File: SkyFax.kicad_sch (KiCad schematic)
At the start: 8 parts, among them J1 RJ11/12, J4 Conn_02x08_Odd_Even, J5 Conn_01x02, J6 Conn_01x02

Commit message: Sent to fab v3.0
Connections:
- net GND: now also J4.16 (Pin_16); no longer J4.15 (Pin_15)
- net SI2494/3V3: now also J4.2 (Pin_2); no longer J4.1 (Pin_1)
- net SI2494/CTS: now also J4.10 (Pin_10); no longer J4.9 (Pin_9)
- net SI2494/DCD: now also J4.14 (Pin_14); no longer J4.13 (Pin_13)
- net SI2494/RI: now also J4.12 (Pin_12); no longer J4.11 (Pin_11)
- net SI2494/RTS: now also J4.8 (Pin_8); no longer J4.7 (Pin_7)
- net SI2494/RXD: now also J4.6 (Pin_6); no longer J4.5 (Pin_5)
- net SI2494/TXD: now also J4.4 (Pin_4); no longer J4.3 (Pin_3)
- net SI3018/RING: now also J1.4, J6.1 (Pin_1); no longer J1.3, J6.2 (Pin_2)
- net SI3018/TIP: now also J1.3, J6.2 (Pin_2); no longer J1.4, J6.1 (Pin_1)
- net USB_Serial/3V3: now also J4.1 (Pin_1); no longer J4.2 (Pin_2)
- net USB_Serial/CTS: now also J4.9 (Pin_9); no longer J4.10 (Pin_10)
- net USB_Serial/DCD: now also J4.13 (Pin_13); no longer J4.14 (Pin_14)
- net USB_Serial/GND: now also J4.15 (Pin_15); no longer J4.16 (Pin_16)
- net USB_Serial/RI: now also J4.11 (Pin_11); no longer J4.12 (Pin_12)
- net USB_Serial/RTS: now also J4.7 (Pin_7); no longer J4.8 (Pin_8)
- net USB_Serial/RXD: now also J4.5 (Pin_5); no longer J4.6 (Pin_6)
- net USB_Serial/TXD: now also J4.3 (Pin_3); no longer J4.4 (Pin_4)
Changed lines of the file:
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@@
+    (stroke (width 0) (type default))
+  )
+  (wire (pts (xy 50.8 47.625) (xy 52.07 47.625))
+    (stroke (width 0) (type default))
+  )
+  (wire (pts (xy 84.455 41.91) (xy 85.09 41.91))
+    (stroke (width 0) (type default))
+  )
+  (wire (pts (xy 48.895 41.91) (xy 52.07 41.91))
+    (stroke (width 0) (type default))
+  )
+  (wire (pts (xy 84.455 30.48) (xy 84.455 41.91))
+    (stroke (width 0) (type default))
+  )
+  (wire (pts (xy 65.405 38.735) (xy 66.04 38.735))
+    (stroke (width 0) (type default))
+  )
+  (wire (pts (xy 33.655 47.625) (xy 35.56 47.625))
+    (stroke (width 0) (type default))
+  )
+  (wire (pts (xy 50.165 32.385) (xy 50.165 34.29))
+    (stroke (width 0) (type default))
+  )
+  (wire (pts (xy 48.26 32.385) (xy 50.165 32.385))
+    (stroke (width 0) (type default))
+  )
+  (wire (pts (xy 34.925 37.465) (xy 35.56 37.465))
+    (stroke (width 0) (type default))
+  )
+  (wire (pts (xy 31.75 36.195) (xy 34.29 36.195))
+    (stroke (width 0) (type default))
+  )
+  (wire (pts (xy 48.26 34.925) (xy 49.53 34.925))
+    (stroke (width 0) (type default))
+  )
+  (wire (pts (xy 48.895 37.465) (xy 48.895 38.1))
+    (stroke (width 0) (type default))
+  )
+  (wire (pts (xy 49.53 45.085) (xy 49.53 43.815))
+    (stroke (width 0) (type default))
+  )
+  (wire (pts (xy 34.925 38.1) (xy 34.925 37.465))
+    (stroke (width 0) (type default))
+  )
+  (wire (pts (xy 33.02 50.165) (xy 35.56 50.165))
+    (stroke (width 0) (type default))
+  )
+  (wire (pts (xy 65.405 40.005) (xy 65.405 38.735))
+    (stroke (width 0) (type default))
+  )
+  (wire (pts (xy 81.915 41.91) (xy 84.455 41.91))
+    (stroke (width 0) (type default))
+  )
+  (wire (pts (xy 98.425 30.48) (xy 98.425 40.005))
+    (stroke (width 0) (type default))
+  )
+  (wire (pts (xy 33.655 45.72) (xy 33.655 47.625))
+    (stroke (width 0) (type default))
+  )
+  (wire (pts (xy 100.965 30.48) (xy 100.965 42.545))
+    (stroke (width 0) (type default))
+  )
+  (wire (pts (xy 48.26 37.465) (xy 48.895 37.465))
+    (stroke (width 0) (type default))
+  )
+  (wire (pts (xy 31.75 43.815) (xy 34.29 43.815))
+    (stroke (width 0) (type default))
+  )
+  (wire (pts (xy 33.02 47.625) (xy 33.02 50.165))
+    (stroke (width 0) (type default))
+  )
+  (wire (pts (xy 31.75 41.91) (xy 34.925 41.91))
+    (stroke (width 0) (type default))
+  )
+  (wire (pts (xy 48.26 45.085) (xy 49.53 45.085))
+    (stroke (width 0) (type default))
+  )
+  (wire (pts (xy 31.75 40.005) (xy 35.56 40.005))
+    (stroke (width 0) (type default))
+  )
+  (wire (pts (xy 34.925 41.91) (xy 34.925 42.545))
+    (stroke (width 0) (type default))
+  )
+  (wire (pts (xy 65.405 41.91) (xy 65.405 43.815))
+    (stroke (width 0) (type default))
+  )
+  (wire (pts (xy 31.75 38.1) (xy 34.925 38.1))
+    (stroke (width 0) (type default))
+  )
+  (wire (pts (xy 31.75 47.625) (xy 33.02 47.625))
+    (stroke (width 0) (type default))
+  )
+  (wire (pts (xy 50.8 50.165) (xy 50.8 47.625))
+    (stroke (width 0) (type default))
+  )
+  (wire (pts (xy 48.26 50.165) (xy 50.8 50.165))
+    (stroke (width 0) (type default))
+  )
+  (wire (pts (xy 34.29 36.195) (xy 34.29 34.925))
+    (stroke (width 0) (type default))
+  )
+  (wire (pts (xy 48.895 42.545) (xy 48.895 41.91))
+    (stroke (width 0) (type default))
+  )
+  (wire (pts (xy 48.26 47.625) (xy 50.165 47.625))
+    (stroke (width 0) (type default))
+  )
+  (wire (pts (xy 31.75 45.72) (xy 33.655 45.72))
+    (stroke (width 0) (type default))
+  )
+  (wire (pts (xy 81.915 38.735) (xy 81.915 40.005))
+    (stroke (width 0) (type default))
+  )
+  (wire (pts (xy 34.29 43.815) (xy 34.29 45.085))
+    (stroke (width 0) (type default))
+  )
+  (wire (pts (xy 85.09 47.625) (xy 83.82 47.625))
+    (stroke (width 0) (type default))
+  )
+  (wire (pts (xy 83.82 47.625) (xy 83.82 50.165))
+    (stroke (width 0) (type default))
+  )
+  (wire (pts (xy 33.655 32.385) (xy 35.56 32.385))
     (stroke (width 0) (type default))
   )
   (wire (pts (xy 48.26 40.005) (xy 52.07 40.005))
-    (stroke (width 0) (type default))
-  )
-  (wire (pts (xy 50.8 47.625) (xy 52.07 47.625))
-    (stroke (width 0) (type default))
-  )
-  (wire (pts (xy 84.455 41.91) (xy 85.09 41.91))
-    (stroke (width 0) (type default))
-  )
-  (wire (pts (xy 48.895 41.91) (xy 52.07 41.91))
-    (stroke (width 0) (type default))
-  )
-  (wire (pts (xy 84.455 30.48) (xy 84.455 41.91))
-    (stroke (width 0) (type default))
-  )
-  (wire (pts (xy 65.405 38.735) (xy 66.04 38.735))
-    (stroke (width 0) (type default))
-  )
-  (wire (pts (xy 33.655 47.625) (xy 35.56 47.625))
-    (stroke (width 0) (type default))
-  )
-  (wire (pts (xy 50.165 32.385) (xy 50.165 34.29))
-    (stroke (width 0) (type default))
-  )
-  (wire (pts (xy 48.26 32.385) (xy 50.165 32.385))
-    (stroke (width 0) (type default))
-  )
-  (wire (pts (xy 34.925 37.465) (xy 35.56 37.465))
-    (stroke (width 0) (type default))
-  )
-  (wire (pts (xy 31.75 36.195) (xy 34.29 36.195))
-    (stroke (width 0) (type default))
-  )
-  (wire (pts (xy 48.26 34.925) (xy 49.53 34.925))
-    (stroke (width 0) (type default))
-  )
-  (wire (pts (xy 48.895 37.465) (xy 48.895 38.1))
-    (stroke (width 0) (type default))
-  )
-  (wire (pts (xy 49.53 45.085) (xy 49.53 43.815))
-    (stroke (width 0) (type default))
-  )
-  (wire (pts (xy 34.925 38.1) (xy 34.925 37.465))
-    (stroke (width 0) (type default))
-  )
-  (wire (pts (xy 33.02 50.165) (xy 35.56 50.165))
-    (stroke (width 0) (type default))
-  )
-  (wire (pts (xy 65.405 40.005) (xy 65.405 38.735))
-    (stroke (width 0) (type default))
-  )
-  (wire (pts (xy 81.915 41.91) (xy 84.455 41.91))
-    (stroke (width 0) (type default))
-  )
-  (wire (pts (xy 98.425 30.48) (xy 98.425 40.005))
-    (stroke (width 0) (type default))
-  )
-  (wire (pts (xy 33.655 45.72) (xy 33.655 47.625))
-    (stroke (width 0) (type default))
-  )
-  (wire (pts (xy 100.965 30.48) (xy 100.965 42.545))
-    (stroke (width 0) (type default))
-  )
-  (wire (pts (xy 48.26 37.465) (xy 48.895 37.465))
-    (stroke (width 0) (type default))
-  )
-  (wire (pts (xy 31.75 43.815) (xy 34.29 43.815))
-    (stroke (width 0) (type default))
-  )
-  (wire (pts (xy 33.02 47.625) (xy 33.02 50.165))
-    (stroke (width 0) (type default))
-  )
-  (wire (pts (xy 31.75 41.91) (xy 34.925 41.91))
-    (stroke (width 0) (type default))
-  )
-  (wire (pts (xy 48.26 45.085) (xy 49.53 45.085))
-    (stroke (width 0) (type default))
-  )
-  (wire (pts (xy 31.75 40.005) (xy 35.56 40.005))
-    (stroke (width 0) (type default))
-  )
-  (wire (pts (xy 34.925 41.91) (xy 34.925 42.545))
-    (stroke (width 0) (type default))
-  )
-  (wire (pts (xy 65.405 41.91) (xy 65.405 43.815))
-    (stroke (width 0) (type default))
-  )
-  (wire (pts (xy 31.75 38.1) (xy 34.925 38.1))
-    (stroke (width 0) (type default))
-  )
-  (wire (pts (xy 31.75 47.625) (xy 33.02 47.625))
-    (stroke (width 0) (type default))
-  )
-  (wire (pts (xy 50.8 50.165) (xy 50.8 47.625))
-    (stroke (width 0) (type default))
-  )
-  (wire (pts (xy 48.26 50.165) (xy 50.8 50.165))
-    (stroke (width 0) (type default))
-  )
-  (wire (pts (xy 34.29 36.195) (xy 34.29 34.925))
-    (stroke (width 0) (type default))
-  )
-  (wire (pts (xy 48.895 42.545) (xy 48.895 41.91))
-    (stroke (width 0) (type default))
-  )
-  (wire (pts (xy 48.26 47.625) (xy 50.165 47.625))
-    (stroke (width 0) (type default))
-  )
-  (wire (pts (xy 31.75 45.72) (xy 33.655 45.72))
-    (stroke (width 0) (type default))
-  )
-  (wire (pts (xy 81.915 38.735) (xy 81.915 40.005))
-    (stroke (width 0) (type default))
-  )
-  (wire (pts (xy 34.29 43.815) (xy 34.29 45.085))
-    (stroke (width 0) (type default))
-  )
-  (wire (pts (xy 85.09 47.625) (xy 83.82 47.625))
-    (stroke (width 0) (type default))
-  )
-  (wire (pts (xy 83.82 47.625) (xy 83.82 50.165))
-    (stroke (width 0) (type default))
-  )
-  (wire (pts (xy 33.655 32.385) (xy 35.56 32.385))
     (stroke (width 0) (type default))
   )
@@
     )
   )
-  (symbol (lib_name "GND_1") (lib_id "power:GND") (at 50.8 50.165 0) (unit 1)
+  (symbol (lib_id "power:GND") (at 50.8 50.165 0) (unit 1)
     (in_bom yes) (on_board yes) (dnp no) (fields_autoplaced)
     (property "Reference" "#PWR032" (at 50.8 56.515 0)
@@
     )
   )
-  (symbol (lib_id "Connector_Generic:Conn_02x08_Odd_Even") (at 43.18 40.005 0) (mirror y) (unit 1)
+  (symbol (lib_id "Connector_Generic:Conn_02x08_Odd_Even") (at 40.64 40.005 0) (unit 1)
     (in_bom yes) (on_board yes) (dnp no)
     (property "Reference" "J4" (at 41.91 29.845 0)
@@
       (effects (font (size 1.27 1.27)) hide)
     )
-    (property "Footprint" "Connector_PinSocket_2.54mm:PinSocket_2x08_P2.54mm_Vertical" (at 43.18 40.005 0)
-      (effects (font (size 1.27 1.27)) hide)
-    )
-    (property "Datasheet" "~" (at 43.18 40.005 0)
+    (property "Footprint" "Connector_PinSocket_2.54mm:PinSocket_2x08_P2.54mm_Vertical" (at 40.64 40.005 0)
+      (effects (font (size 1.27 1.27)) hide)
+    )
+    (property "Datasheet" "~" (at 40.64 40.005 0)
       (effects (font (size 1.27 1.27)) hide)
     )
@@
       (effects (font (size 1.27 1.27)) (justify left))
     )
-    (pin "RING" bidirectional (at 97.79 41.91 0)
-      (effects (font (size 1.27 1.27)) (justify right))
-    )
-    (pin "TIP" bidirectional (at 97.79 40.005 0)
-      (effects (font (size 1.27 1.27)) (justify right))
-    )
+    (pin "RING" bidirectional (at 97.79 40.005 0)
+      (effects (font (size 1.27 1.27)) (justify right))
+    )
+    (pin "TIP" bidirectional (at 97.79 41.91 0)
+      (effects (font (size 1.27 1.27)) (justify right))
+    )

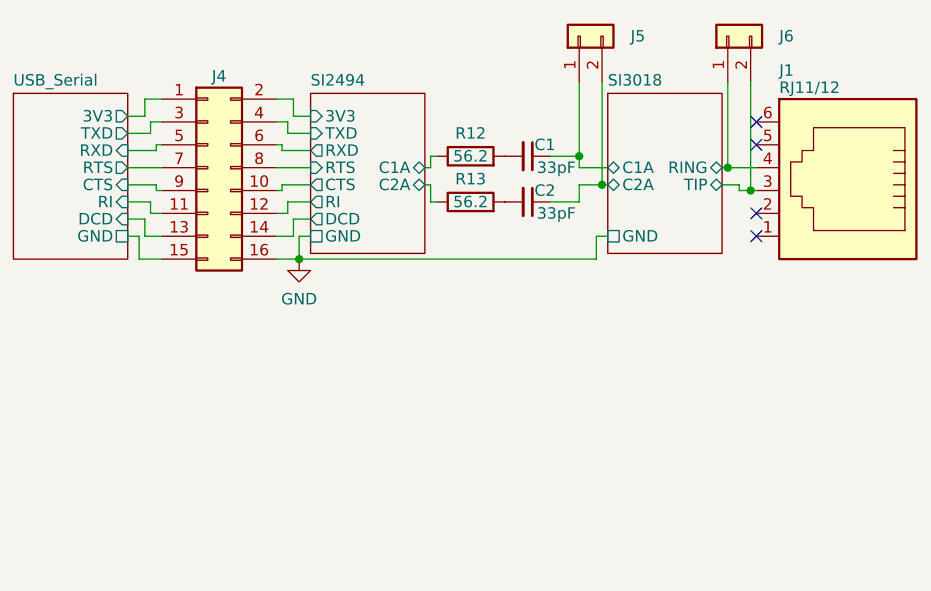
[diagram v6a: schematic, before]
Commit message: Version 3.0 minor BOM changes
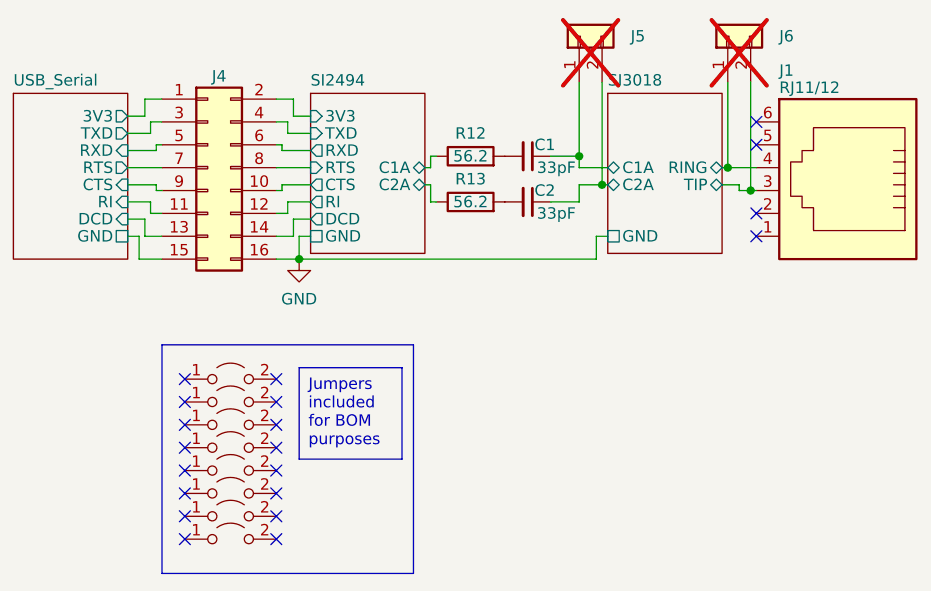
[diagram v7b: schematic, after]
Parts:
- added JP1, JP2, JP3, JP4, JP5, JP6, JP7, JP8: Jumper_2_Open, symbol Jumper:Jumper_2_Open
- J4: footprint Connector_PinSocket_2.54mm:PinSocket_2x08_P2.54mm_Vertical -> Connector_PinHeader_2.54mm:PinHeader_2x08_P2.54mm_Vertical; DIGIKEY (none) -> 609-3364-ND
- J5, J6: now not fitted; now left out of the parts list
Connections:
- no-connect marks 4 -> 20

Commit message: Version 3.0 ERC/DRC fixes
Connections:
- net GND: now also J4.15 (Pin_15); no longer J4.16 (Pin_16)
- net SI2494/3V3: now also J4.1 (Pin_1); no longer J4.2 (Pin_2)
- net SI2494/CTS: now also J4.9 (Pin_9); no longer J4.10 (Pin_10)
- net SI2494/DCD: now also J4.13 (Pin_13); no longer J4.14 (Pin_14)
- net SI2494/RI: now also J4.11 (Pin_11); no longer J4.12 (Pin_12)
- net SI2494/RTS: now also J4.7 (Pin_7); no longer J4.8 (Pin_8)
- net SI2494/RXD: now also J4.5 (Pin_5); no longer J4.6 (Pin_6)
- net SI2494/TXD: now also J4.3 (Pin_3); no longer J4.4 (Pin_4)
- net USB_Serial/3V3: now also J4.2 (Pin_2); no longer J4.1 (Pin_1)
- net USB_Serial/CTS: now also J4.10 (Pin_10); no longer J4.9 (Pin_9)
- net USB_Serial/DCD: now also J4.14 (Pin_14); no longer J4.13 (Pin_13)
- net USB_Serial/GND: now also J4.16 (Pin_16); no longer J4.15 (Pin_15)
- net USB_Serial/RI: now also J4.12 (Pin_12); no longer J4.11 (Pin_11)
- net USB_Serial/RTS: now also J4.8 (Pin_8); no longer J4.7 (Pin_7)
- net USB_Serial/RXD: now also J4.6 (Pin_6); no longer J4.5 (Pin_5)
- net USB_Serial/TXD: now also J4.4 (Pin_4); no longer J4.3 (Pin_3)
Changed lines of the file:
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@@
+    (stroke (width 0) (type default))
+  )
+  (wire (pts (xy 31.75 40.005) (xy 35.56 40.005))
     (stroke (width 0) (type default))
   )
@@
   )
   (wire (pts (xy 48.26 45.085) (xy 49.53 45.085))
-    (stroke (width 0) (type default))
-  )
-  (wire (pts (xy 31.75 40.005) (xy 35.56 40.005))
     (stroke (width 0) (type default))
   )
@@
     )
   )
-  (symbol (lib_id "Connector_Generic:Conn_02x08_Odd_Even") (at 40.64 40.005 0) (unit 1)
+  (symbol (lib_id "Connector_Generic:Conn_02x08_Odd_Even") (at 43.18 40.005 0) (mirror y) (unit 1)
     (in_bom yes) (on_board yes) (dnp no)
     (property "Reference" "J4" (at 41.91 29.845 0)
@@
       (effects (font (size 1.27 1.27)) hide)
     )
-    (property "Footprint" "Connector_PinHeader_2.54mm:PinHeader_2x08_P2.54mm_Vertical" (at 40.64 40.005 0)
-      (effects (font (size 1.27 1.27)) hide)
-    )
-    (property "Datasheet" "~" (at 40.64 40.005 0)
-      (effects (font (size 1.27 1.27)) hide)
-    )
-    (property "DIGIKEY" "609-3364-ND" (at 40.64 40.005 0)
-      (effects (font (size 1.27 1.27)) hide)
-    )
+    (property "Footprint" "Connector_PinHeader_2.54mm:PinHeader_2x08_P2.54mm_Vertical" (at 43.18 40.005 0)
+      (effects (font (size 1.27 1.27)) hide)
+    )
+    (property "Datasheet" "~" (at 43.18 40.005 0)
+      (effects (font (size 1.27 1.27)) hide)
+    )
+    (property "DIGIKEY" "609-3364-ND" (at 43.18 40.005 0)
+      (effects (font (size 1.27 1.27)) hide)
+    )
